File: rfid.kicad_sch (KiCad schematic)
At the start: 0 parts

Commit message: amp and sd sheets revision 1
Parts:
- added C12, C13, C16, C17, C18, C2, C4: C, symbol Device:C
- added R1, R6: R, symbol Device:R
- added R8: 100, symbol Device:R
- added U3: PN5321A3HN_C1xx, Package_DFN_QFN:HVQFN-40-1EP_6x6mm_P0.5mm_EP4.1x4.1mm, symbol RF_NFC:PN5321A3HN_C1xx
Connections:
- new net: R1.1, R6.2, U3.38 (~{RSTPD})
- new net: R8.2, U3.26 (~{RSTOUT})
- new net GND: C12.2, C13.2, C2.2, C4.2, R6.1, U3.1 (DVSS), U3.11 (AVSS), U3.18 (TESTEN), U3.3 (TVSS1), U3.7 (TVSS2)
- new net IRQ: R8.1
- new net MOSI/SDA/TX: U3.28 (MOSI/SDA/HSU_TX)
- new net RSTOUT_N: U3.25 (P70_IRQ)
- new net SSEL/SCL/RX: U3.27 (NSS/P50_SCL/HSU_RX)
- new net VDD33: C12.1, C13.1, C2.1, C4.1, R1.2, U3.23 (PVDD), U3.39 (DVDD), U3.40 (VBAT)
- no-connect marks 0 -> 16

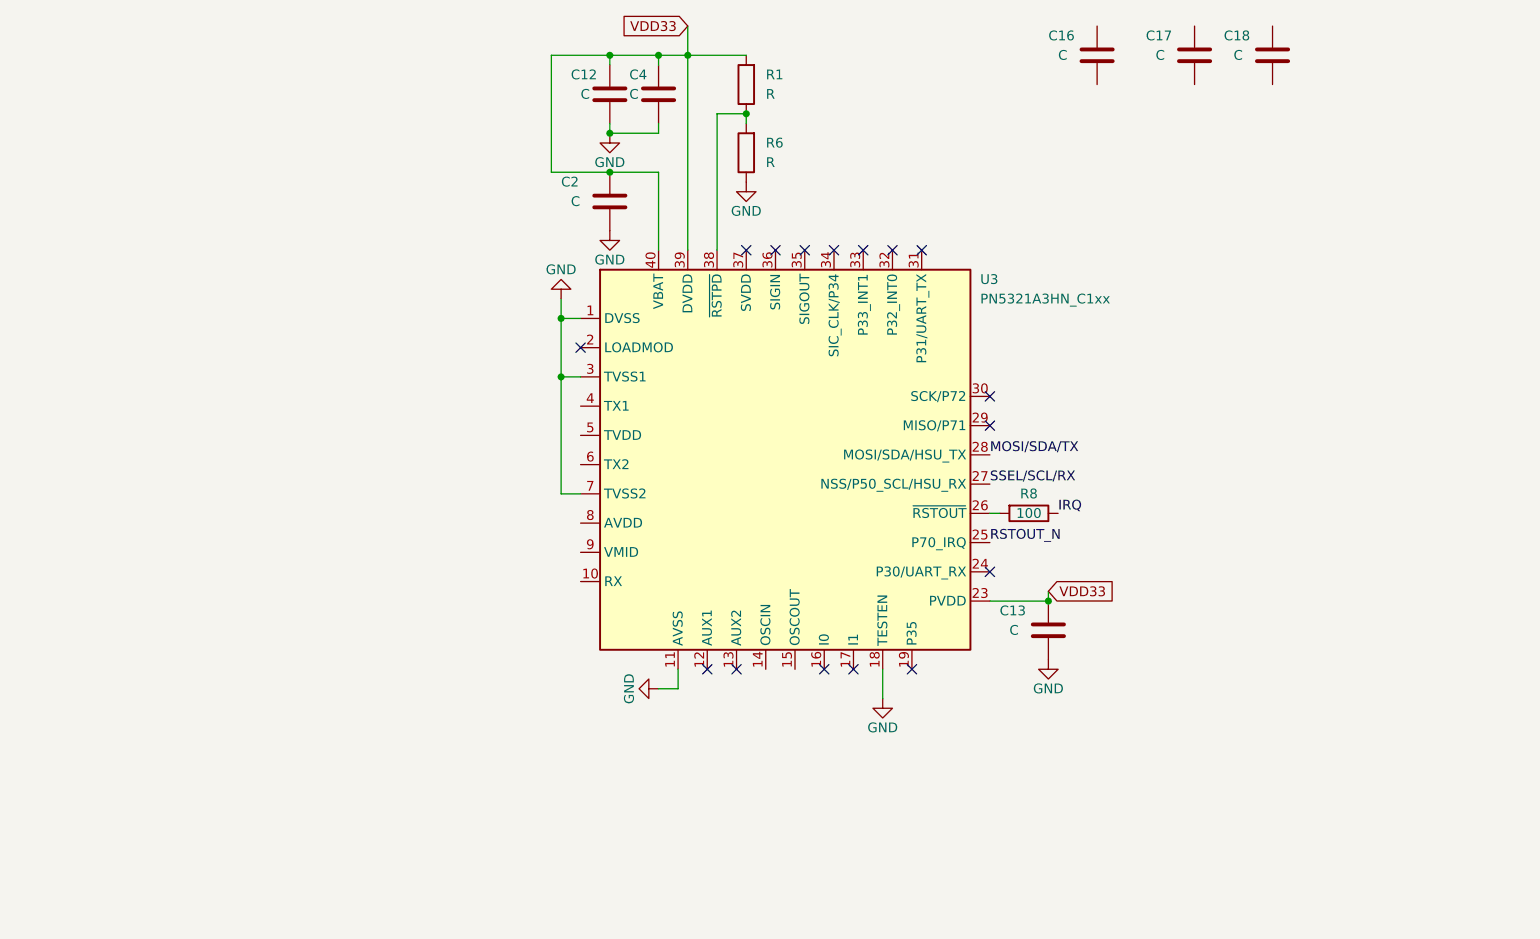
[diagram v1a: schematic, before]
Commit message: rfid revision 1 sch
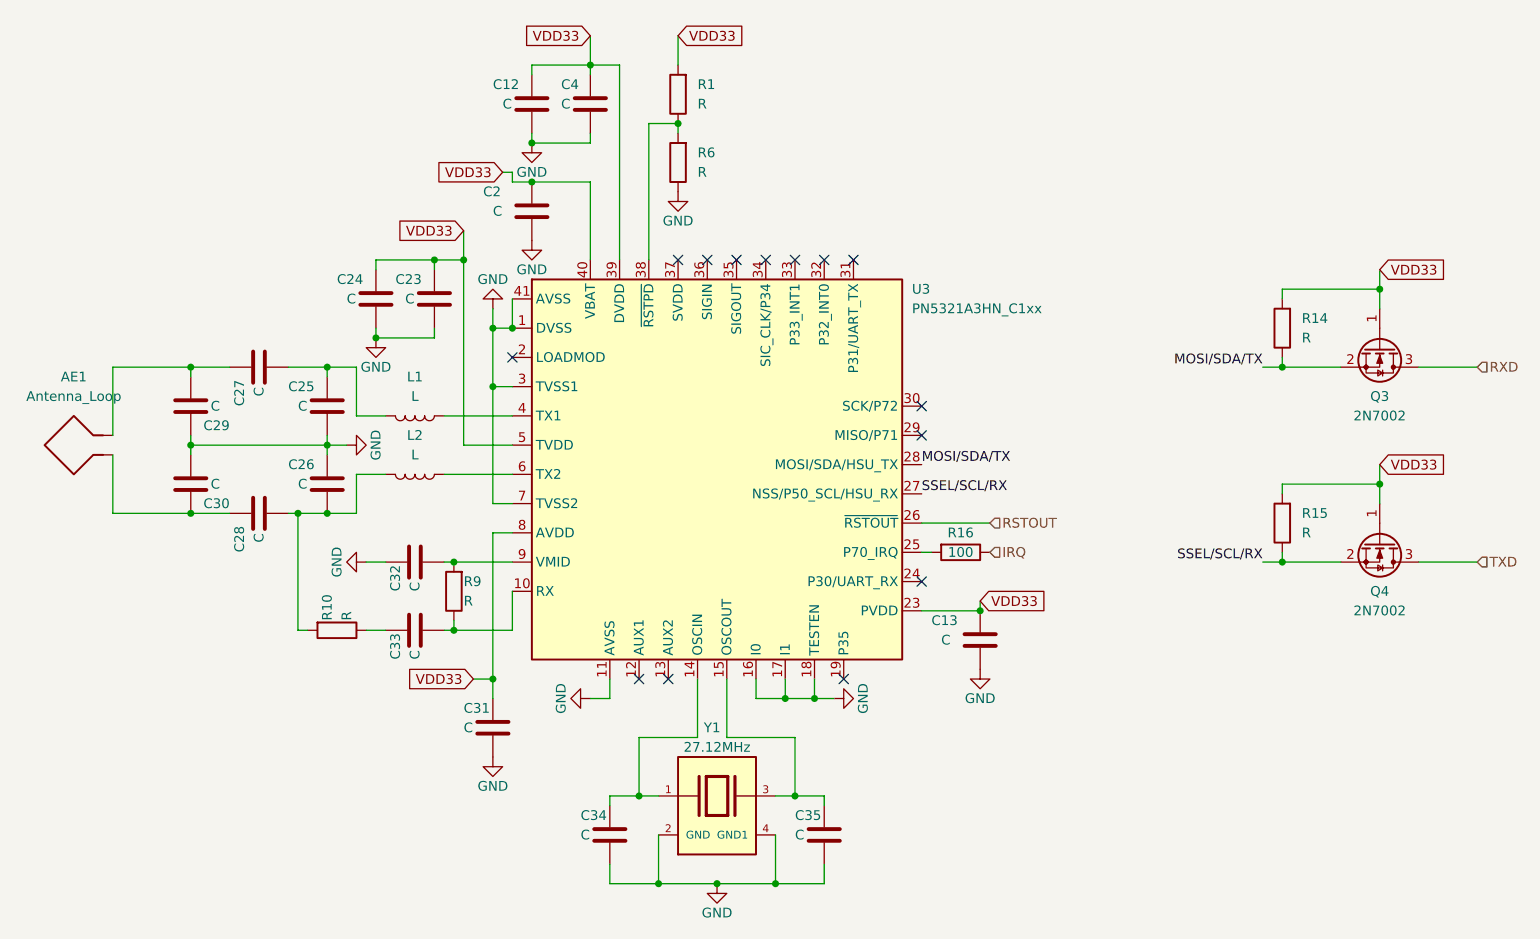
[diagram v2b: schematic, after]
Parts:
- removed C16, C17, C18: C, symbol Device:C
- removed R8: 100, symbol Device:R
- added AE1: Antenna_Loop, symbol Device:Antenna_Loop
- added C23, C24, C25, C26, C27, C28, C29, C30, C31, C32, C33, C34, C35: C, symbol Device:C
- added L1, L2: L, symbol Device:L
- added Q3, Q4: 2N7002, Package_TO_SOT_SMD:SOT-23, symbol Transistor_FET:2N7002
- added R10, R14, R15, R9: R, symbol Device:R
- added R16: 100, symbol Device:R
- added Y1: 27.12MHz, ABM8-27.120MHz-10-B1U-T:XTAL_ABM8-27.120MHz-10-B1U-T, symbol ABM8-27.120MHz-10-B1U-T:ABM8-27.120MHz-10-B1U-T
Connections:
- net GND: now also U3.16 (I0), U3.17 (I1), U3.41 (AVSS), C23.2, C24.2, C25.2, C26.1, C29.1, C30.2, C31.2, C32.1, C34.2, C35.2, Y1.2 (GND), Y1.4 (GND1)
- net IRQ: now also R16.1
- net MOSI/SDA/TX: now also Q3.2 (S), R14.1
- net SSEL/SCL/RX: now also Q4.2 (S), R15.1
- net VDD33: now also U3.5 (TVDD), U3.8 (AVDD), C23.1, C24.1, C31.1, Q3.1 (G), Q4.1 (G), R14.2, R15.2
- net RSTOUT: now reaches U3.26 (~{RSTOUT})
- net at U3.10 (RX): now also C33.2, R9.1
- net at U3.14 (OSCIN): now also C34.1, Y1.1
- net at U3.15 (OSCOUT): now also C35.1, Y1.3
- net at U3.4 (TX1): now also L1.1
- net at U3.6 (TX2): now also L2.1
- net at U3.9 (VMID): now also C32.2, R9.2
- net RSTOUT_N: no longer names the net of U3.25 (P70_IRQ)
- net RSTOUT_N: now also R16.2
- new net: AE1.1, C28.1, C30.1
- new net: C26.2, C28.2, L2.2, R10.2
- new net: AE1.2, C27.1, C29.2
- new net: C25.1, C27.2, L1.2
- new net: C33.1, R10.1
- new net RXD: Q3.3 (D)
- new net TXD: Q4.3 (D)
- no-connect marks 16 -> 14
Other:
- company: (none) -> C. Boerner
- title: (none) -> RFID Module
- moved on the sheet: C12, C13, C2, C4, R1, R6
